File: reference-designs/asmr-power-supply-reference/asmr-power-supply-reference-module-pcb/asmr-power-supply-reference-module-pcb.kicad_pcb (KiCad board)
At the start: 2 copper layers, 136 x 71 mm, 1 part

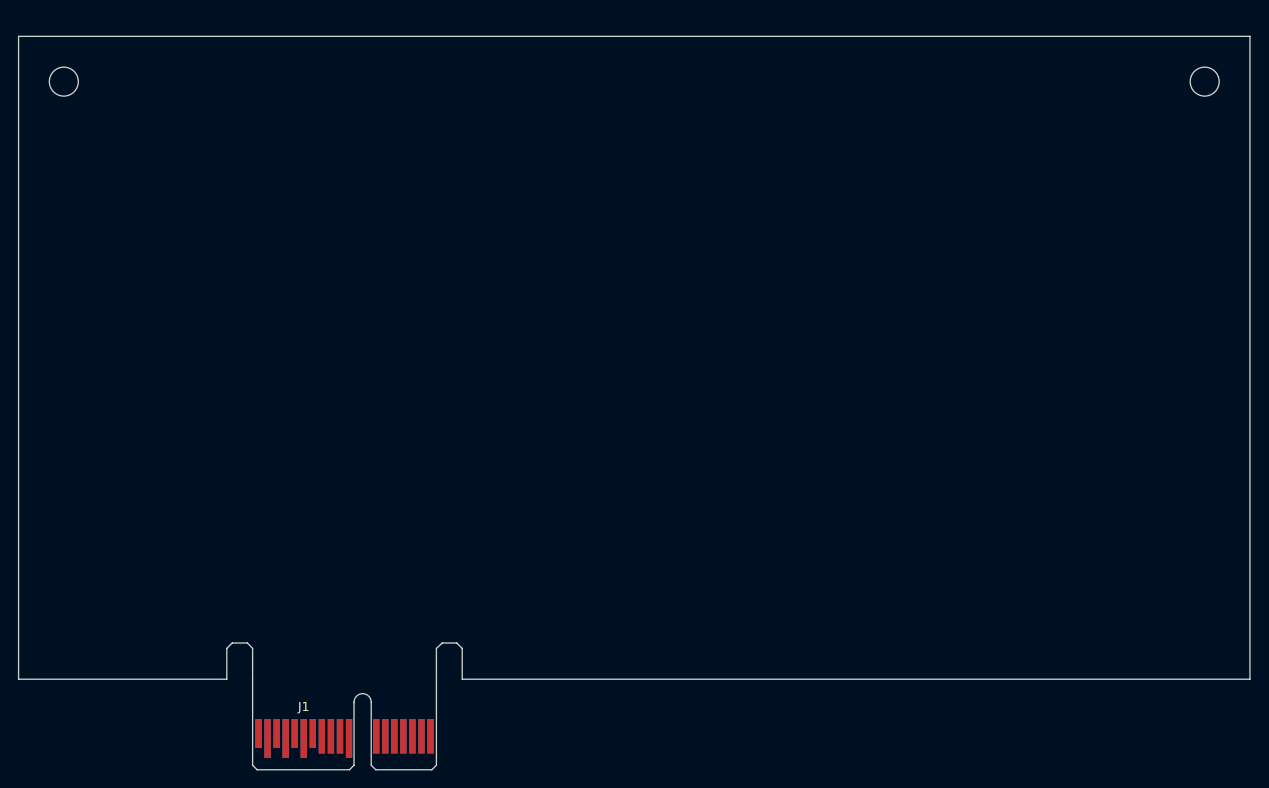
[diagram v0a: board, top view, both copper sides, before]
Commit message: First pass on the power supply module.
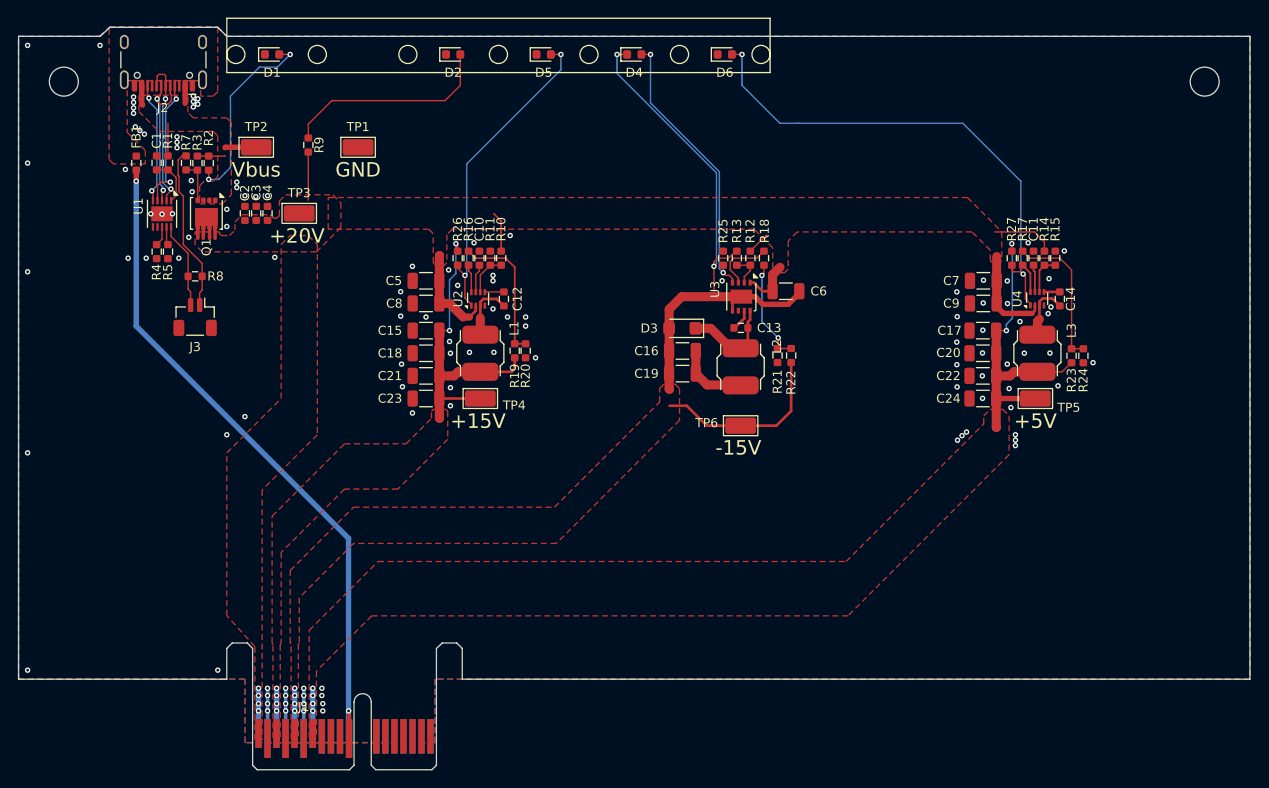
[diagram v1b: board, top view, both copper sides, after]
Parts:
- added C1: 1uF/50V, CM_Resistor_Capacitor:C_0603_1608Metric, F.Cu at (97.2, 58.0)
- added C10: 22nF, CM_Resistor_Capacitor:C_0603_1608Metric, F.Cu at (132.9, 68.5)
- added C11: 22nF, CM_Resistor_Capacitor:C_0603_1608Metric, F.Cu at (194.1, 68.5)
- added C12: 0.1uF, CM_Resistor_Capacitor:C_0603_1608Metric, F.Cu at (135.6, 73.0)
- added C13: 0.1uF, CM_Resistor_Capacitor:C_0603_1608Metric, F.Cu at (161.8, 76.2)
- added C14: 0.1uF, CM_Resistor_Capacitor:C_0603_1608Metric, F.Cu at (197.0, 73.0)
- added C15: 10uF, Capacitor_SMD:C_1206_3216Metric, F.Cu at (127.0, 76.5)
- added C16: 10uF, Capacitor_SMD:C_1206_3216Metric, F.Cu at (155.3, 78.8)
- added C17: 10uF, Capacitor_SMD:C_1206_3216Metric, F.Cu at (188.5, 76.5)
- added C18: 10uF, Capacitor_SMD:C_1206_3216Metric, F.Cu at (127.0, 79.0)
- added C19: 10uF, Capacitor_SMD:C_1206_3216Metric, F.Cu at (155.3, 81.2)
- added C2: 4.7uF/50V, CM_Resistor_Capacitor:C_0603_1608Metric, F.Cu at (107.0, 63.5)
- added C20: 10uF, Capacitor_SMD:C_1206_3216Metric, F.Cu at (188.5, 79.0)
- added C21: 10uF, Capacitor_SMD:C_1206_3216Metric, F.Cu at (127.0, 81.5)
- added C22: 10uF, Capacitor_SMD:C_1206_3216Metric, F.Cu at (188.5, 81.5)
- added C23: 10uF, Capacitor_SMD:C_1206_3216Metric, F.Cu at (127.0, 84.0)
- added C24: 10uF, Capacitor_SMD:C_1206_3216Metric, F.Cu at (188.5, 84.0)
- added C3: 4.7uF/50V, CM_Resistor_Capacitor:C_0603_1608Metric, F.Cu at (108.2, 63.5)
- added C4: 4.7uF/50V, CM_Resistor_Capacitor:C_0603_1608Metric, F.Cu at (109.5, 63.5)
- added C5: 10uF, Capacitor_SMD:C_1206_3216Metric, F.Cu at (127.0, 71.0)
- added C6: 10uF/50V, Capacitor_SMD:C_1206_3216Metric, F.Cu at (166.8, 72.2)
- added C7: 10uF, Capacitor_SMD:C_1206_3216Metric, F.Cu at (188.6, 71.0)
- added C8: 10uF, Capacitor_SMD:C_1206_3216Metric, F.Cu at (127.0, 73.5)
- added C9: 10uF, Capacitor_SMD:C_1206_3216Metric, F.Cu at (188.6, 73.5)
- added D1: BLU, LED_SMD:LED_0603_1608Metric, F.Cu at (110.0, 46.0)
- added D2: BLU, LED_SMD:LED_0603_1608Metric, F.Cu at (130.0, 46.0)
- added D3: 60V, Diode_SMD:D_SMF, F.Cu at (155.3, 76.2)
- added D4: GRN, LED_SMD:LED_0603_1608Metric, F.Cu at (150.0, 46.0)
- added D5: GRN, LED_SMD:LED_0603_1608Metric, F.Cu at (140.0, 46.0)
- added D6: GRN, LED_SMD:LED_0603_1608Metric, F.Cu at (160.0, 46.0)
- added FB1: 100@1M, CM_Resistor_Capacitor:R_0603_1608Metric, F.Cu at (95.0, 58.0)
- added J2: USB_C_Receptacle_USB2.0_14P, Connector_USB:USB_C_Receptacle_HCTL_HC-TYPE-C-16P-01A, F.Cu at (98.0, 45.7)
- added J3: PWR-SW, Connector_JST:JST_SH_BM02B-SRSS-TB_1x02-1MP_P1.00mm_Vertical, F.Cu at (101.5, 75.0)
- added L1: 15uH, CM_Inductor:SRN5040, F.Cu at (133.0, 79.0)
- added L2: 15uH, CM_Inductor:SRN5040, F.Cu at (161.8, 80.5)
- added L3: 10uH, CM_Inductor:SRN5040, F.Cu at (194.5, 79.0)
- added Q1: DMP3036SFV, Package_SON:VSON-8_3.3x3.3mm_P0.65mm_NexFET, F.Cu at (102.8, 63.5)
- added R1: 10R, CM_Resistor_Capacitor:R_0603_1608Metric, F.Cu at (98.5, 58.0)
- added R10: 500K, CM_Resistor_Capacitor:R_0603_1608Metric, F.Cu at (135.3, 68.5)
- added R11: 49.9K, CM_Resistor_Capacitor:R_0603_1608Metric, F.Cu at (134.1, 68.5)
- added R12: 500K, CM_Resistor_Capacitor:R_0603_1608Metric, F.Cu at (162.8, 68.5)
- added R13: 27K, CM_Resistor_Capacitor:R_0603_1608Metric, F.Cu at (161.3, 68.5)
- added R14: 500K, CM_Resistor_Capacitor:R_0603_1608Metric, F.Cu at (195.3, 68.5)
- added R15: 49.9K, CM_Resistor_Capacitor:R_0603_1608Metric, F.Cu at (196.5, 68.5)
- added R16: 10.0K, CM_Resistor_Capacitor:R_0603_1608Metric, F.Cu at (131.7, 68.5)
- added R17: 10.0K, CM_Resistor_Capacitor:R_0603_1608Metric, F.Cu at (192.9, 68.5)
- added R18: 0R, CM_Resistor_Capacitor:R_0603_1608Metric, F.Cu at (164.3, 68.5)
- added R19: 237K, CM_Resistor_Capacitor:R_0603_1608Metric, F.Cu at (136.8, 78.7)
- added R2: 1.8K, CM_Resistor_Capacitor:R_0603_1608Metric, F.Cu at (103.0, 58.0)
- added R20: 8.2K, CM_Resistor_Capacitor:R_0603_1608Metric, F.Cu at (138.0, 78.7)
- added R21: 177K, CM_Resistor_Capacitor:R_0603_1608Metric, F.Cu at (165.8, 79.2)
- added R22: 10.0K, CM_Resistor_Capacitor:R_0603_1608Metric, F.Cu at (167.3, 79.2)
- added R23: 90.9K, CM_Resistor_Capacitor:R_0603_1608Metric, F.Cu at (198.3, 79.3)
- added R24: 10.0K, CM_Resistor_Capacitor:R_0603_1608Metric, F.Cu at (199.6, 79.3)
- added R25: 1.8K, CM_Resistor_Capacitor:R_0603_1608Metric, F.Cu at (159.8, 68.5)
- added R26: 1.8K, CM_Resistor_Capacitor:R_0603_1608Metric, F.Cu at (130.5, 68.5)
- added R27: 680R, CM_Resistor_Capacitor:R_0603_1608Metric, F.Cu at (191.7, 68.5)
- added R3: 49.9K, CM_Resistor_Capacitor:R_0603_1608Metric, F.Cu at (101.8, 58.0)
- added R4: NS, CM_Resistor_Capacitor:R_0603_1608Metric, F.Cu at (97.2, 67.8)
- added R5: NS, CM_Resistor_Capacitor:R_0603_1608Metric, F.Cu at (98.5, 67.8)
- added R7: 5.1K, CM_Resistor_Capacitor:R_0603_1608Metric, F.Cu at (100.5, 58.0)
- added R8: 0R, CM_Resistor_Capacitor:R_0603_1608Metric, F.Cu at (101.5, 70.5)
- added R9: 1.8K, CM_Resistor_Capacitor:R_0603_1608Metric, F.Cu at (114.0, 56.0)
- added TP1: GND, TestPoint:TestPoint_Keystone_5015_Micro_Mini, F.Cu at (119.5, 56.2)
- added TP2: Vbus, TestPoint:TestPoint_Keystone_5015_Micro_Mini, F.Cu at (108.2, 56.2)
- added TP3: +20V, TestPoint:TestPoint_Keystone_5015_Micro_Mini, F.Cu at (113.0, 63.5)
- added TP4: +15V, TestPoint:TestPoint_Keystone_5015_Micro_Mini, F.Cu at (133.0, 84.0)
- added TP5: +5V, TestPoint:TestPoint_Keystone_5015_Micro_Mini, F.Cu at (194.3, 84.0)
- added TP6: -15V, TestPoint:TestPoint_Keystone_5015_Micro_Mini, F.Cu at (161.8, 87.0)
- added U1: HUSB238, Package_DFN_QFN:DFN-10-1EP_3x3mm_P0.5mm_EP1.65x2.38mm, F.Cu at (97.8, 63.6)
- added U2: MP2328C, Package_TO_SOT_SMD:SOT-583-8, F.Cu at (132.8, 73.0)
- added U3: MCP1365, Package_DFN_QFN:DFN-8-1EP_3x3mm_P0.65mm_EP1.55x2.4mm, F.Cu at (161.8, 72.8)
- added U4: MP2328C, Package_TO_SOT_SMD:SOT-583-8, F.Cu at (194.5, 73.0)
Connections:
- net +24V renamed +20V
- net GND renamed GND_CH
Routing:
- net -15V: track 0.00 -> 88.3 mm, vias 0 -> 6
- net GNDS: track 0.00 -> 75.6 mm, vias 0 -> 2
- net +20V: track 0.00 -> 63.4 mm, vias 0 -> 4
- net /PG5: track 0.00 -> 55.9 mm, vias 0 -> 2
- net +5V: track 0.00 -> 41.1 mm, vias 0 -> 6
- net +15V: track 0.00 -> 41.0 mm, vias 0 -> 6
- net /PG15P: track 0.00 -> 35.0 mm, vias 0 -> 2
- net /PG15N: track 0.00 -> 31.0 mm, vias 0 -> 2
- net GND_CH: track 0.00 -> 24.6 mm, vias 0 -> 115
- net Net-(D2-A): track 0.00 -> 23.5 mm
- net Net-(D1-A): track 0.00 -> 21.6 mm, vias 0 -> 2
- net Net-(J3-Pin_1): track 0.00 -> 18.3 mm
- net Net-(U1-D-): track 0.00 -> 17.2 mm, vias 0 -> 2
- net Net-(U1-D+): track 0.00 -> 16.8 mm, vias 0 -> 2
- net /FB5: track 0.00 -> 16.3 mm
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- added copper zone on F.Cu, net +15V
- added copper zone on F.Cu, net +20V
- added copper zone on F.Cu, net +5V
- added copper zone on F.Cu, net -15V
- added copper zone on F.Cu, net /SHIELD
- added copper zone on F.Cu, net /Vbus
- added copper zone on B.Cu, net GND_CH
- added copper zone on F.Cu, net GND_CH
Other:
- board size 136 x 71 mm -> 136 x 72 mm
- rule pad_to_mask_clearance: 0 -> 0.0508

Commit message: Update design with 64 pin PCI connector.
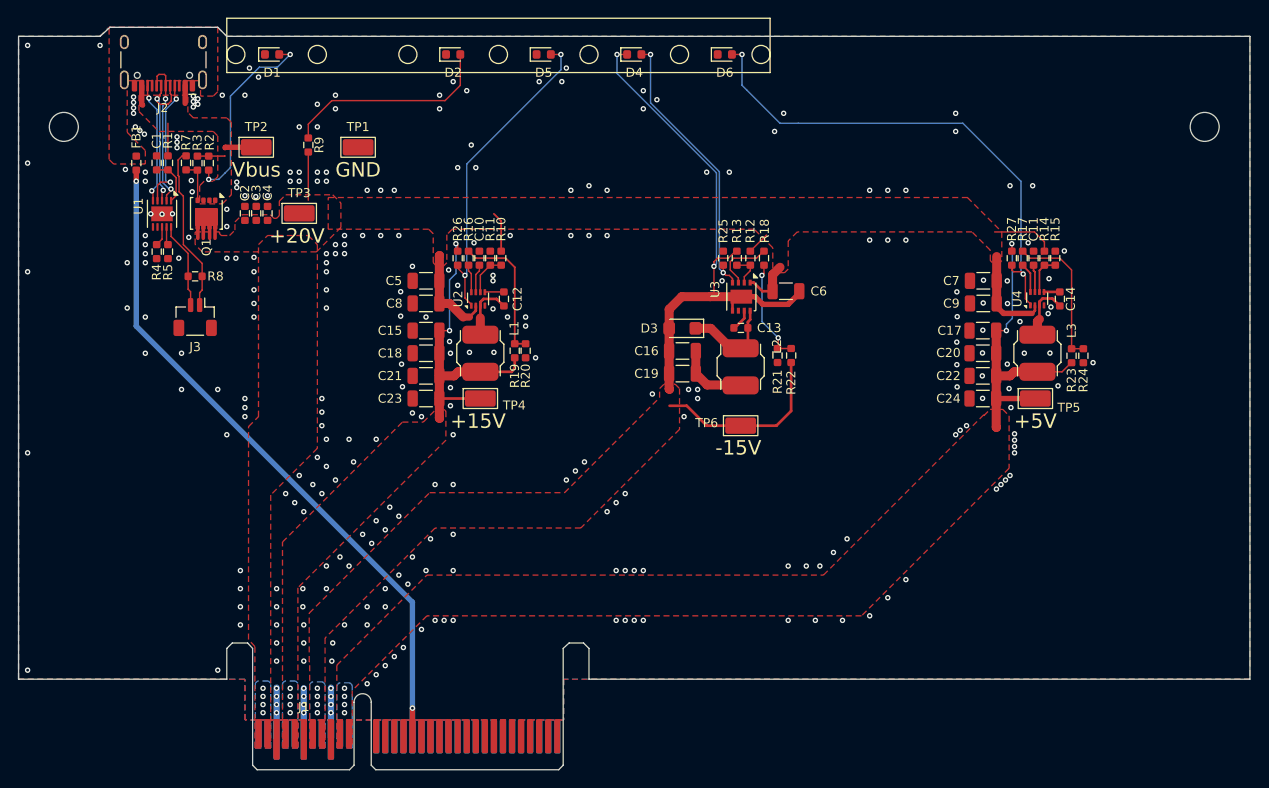
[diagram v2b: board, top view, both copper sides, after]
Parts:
- J1: footprint CM_Connector_Edge:ASMR-Edge-36 -> CM_Connector_Edge:ASMR-Edge-64
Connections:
- J1 pad A10: unconnected-(J1-CV-PadA10) -> +5V
- J1 pad A11: GNDS -> +5V
- J1 pad A16: unconnected-(J1-Patch8-PadA16) -> GNDS
- J1 pad A2: GND_CH -> +20V
- J1 pad A3: +15V -> GND_CH
- J1 pad A4: GND_CH -> +15V
- J1 pad A5: -15V -> +15V
- J1 pad A7: +5V -> -15V
- J1 pad A8: unconnected-(J1-ComA-SCK-PadA8) -> -15V
- J1 pad A9: unconnected-(J1-ComB-SCK-PadA9) -> GND_CH
- J1 pad B10: unconnected-(J1-Gate-PadB10) -> +5V
- J1 pad B11: GNDS -> +5V
- J1 pad B16: unconnected-(J1-Patch7-PadB16) -> GNDS
- J1 pad B2: GND_CH -> +20V
- J1 pad B3: +15V -> GND_CH
- J1 pad B4: GND_CH -> +15V
- J1 pad B5: -15V -> +15V
- J1 pad B7: +5V -> -15V
- J1 pad B8: unconnected-(J1-ComA-SDA-PadB8) -> -15V
- J1 pad B9: unconnected-(J1-ComB-SDA-PadB9) -> GND_CH
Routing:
- net -15V: track 88.3 -> 83.3 mm
- net +5V: track 41.1 -> 36.1 mm
- net +20V: track 63.4 -> 58.4 mm
- net +15V: track 41.0 -> 36.0 mm
- net GNDS: track 75.6 -> 78.3 mm
- net GND_CH: vias 115 -> 298
- added copper zone on B.Cu, net +15V
- added copper zone on B.Cu, net +20V
- added copper zone on B.Cu, net +5V
- added copper zone on B.Cu, net -15V
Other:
- outline, holes or cut-outs redrawn
- board text removed: "Card Socket"
- board text removed: "Chassis Inner Wall"
- board text removed: "Courtyard Shape: Suggested Bracket to hold PCB to Face Plate (2 places)"
- board text removed: "Maximum Allowed PCB Perimeter"
- board text removed: "PCB Backplane"
- board text removed: "Rail"
- board text removed: "Rail Clearance"
- board text removed: "Space Reserved for Chassis Features."
